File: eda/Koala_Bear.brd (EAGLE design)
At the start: 59.3 x 40 mm, 27 parts

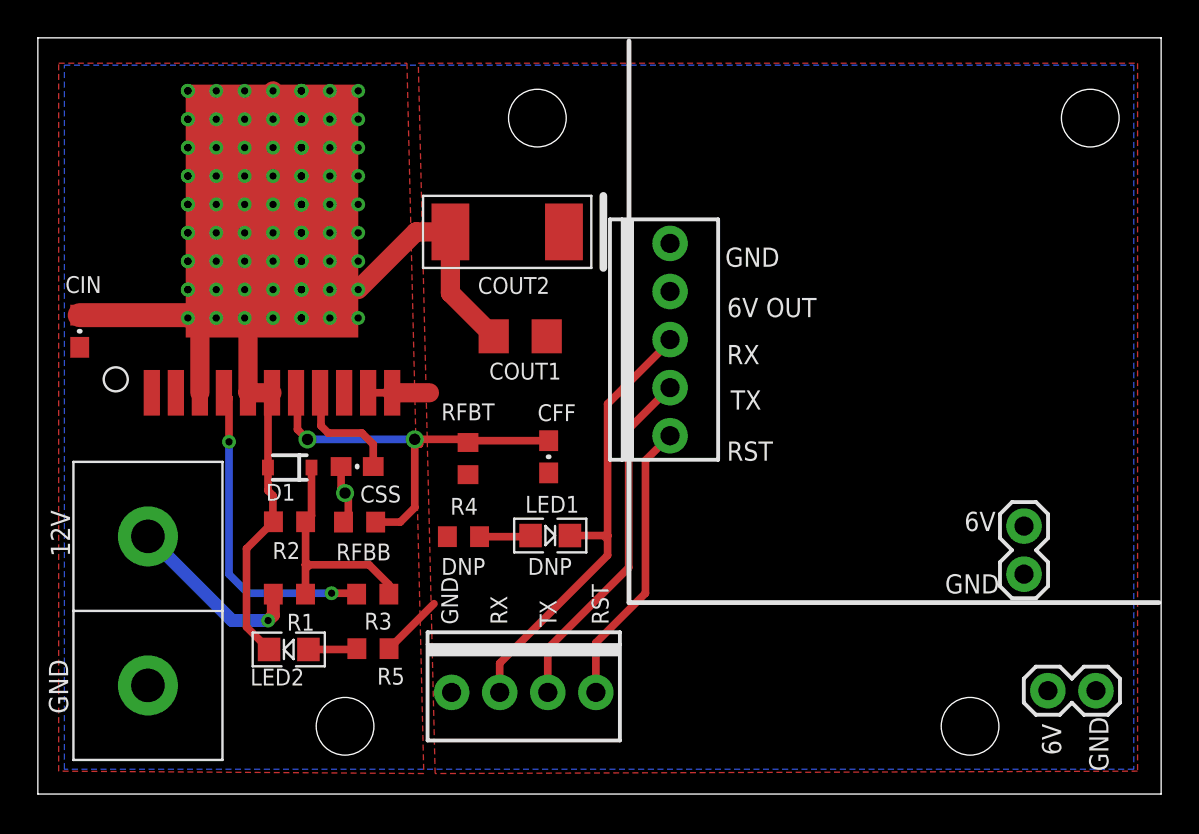
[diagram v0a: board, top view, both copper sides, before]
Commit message: Made Koala smaller
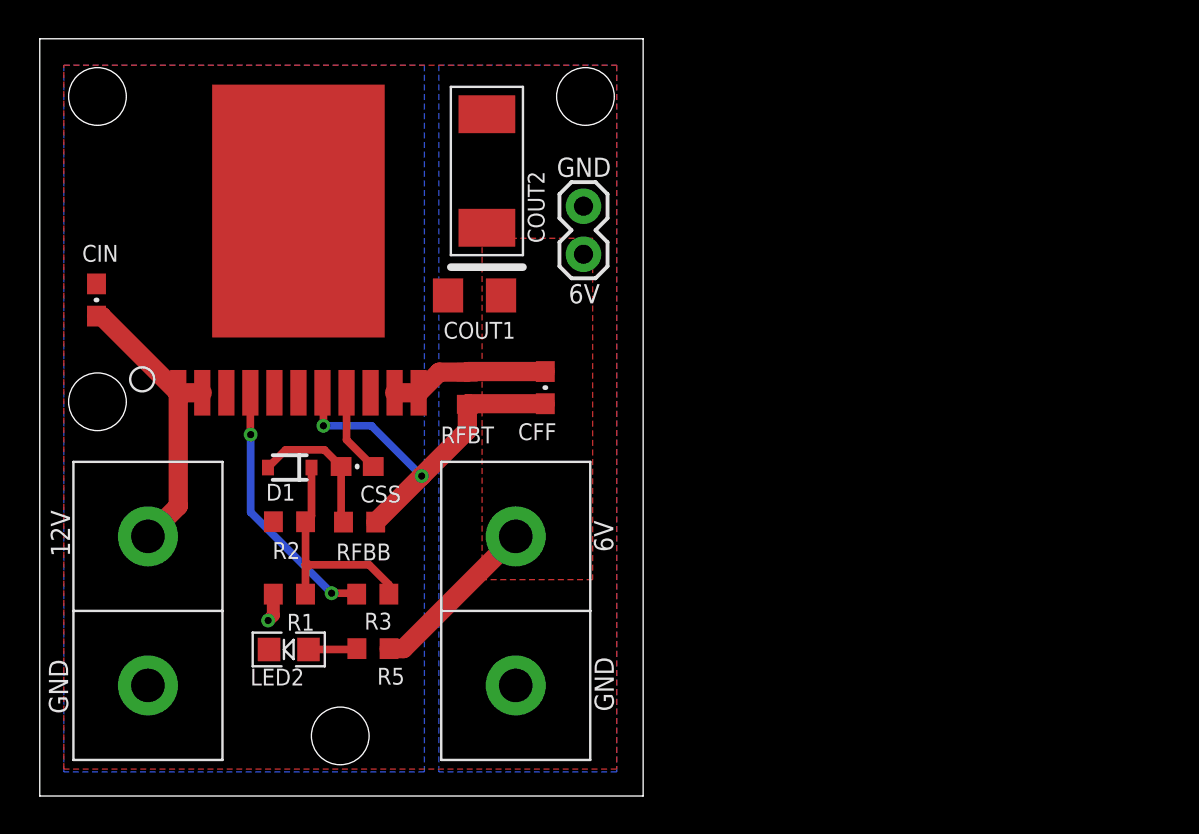
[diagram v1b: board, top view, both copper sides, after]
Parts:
- removed LED1: GRN, pie:LED-0805
- removed MSTRO_PINS: (no value), pie_new:1X04-MTA
- removed MSTRO_PWR: (no value), pie:1X05-MTA
- removed R4: 330, pie:R0603
- removed SERVO_PWR_6: (no value), pie:1X02
- added PWR1: ANDERSONVERTICAL, pie:ANDERSON_VERTICAL
- moved U$3 49.2 mm to (3.05, 20.8)
- moved SERVO_PWR_12 35.5 mm to (28.7, 29.9), turned to 270 degrees
- moved U$2 26.7 mm to (28.8, 37.0)
- moved U$11 25.9 mm to (20.8, 33.0)
- moved U$4 23.3 mm to (3.05, 37.0)
- moved U$10 19.9 mm to (5.06, 29.2)
- moved RFBT 3.72 mm to (22.6, 21.5), turned to 90 degrees
- moved CFF 3.66 mm to (26.7, 21.6), turned to 270 degrees
- moved COUT2 3.39 mm to (23.6, 33.0), turned to 90 degrees
- moved COUT1 3.24 mm to (23.0, 26.4)
- moved CIN 1.88 mm to (3.00, 26.2)
- moved U$1 1.40 mm to (13.7, 30.9)
- moved U$5 0.57 mm to (15.9, 3.17)
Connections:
- removed net N$1: LED1.A, R4.1
- removed net RST: MSTRO_PINS.4, MSTRO_PWR.1
- removed net RX: LED1.C, MSTRO_PINS.2, MSTRO_PWR.3
- removed net TX: MSTRO_PINS.3, MSTRO_PWR.2
- net GND: now also PWR1.PIN1; no longer MSTRO_PINS.1, MSTRO_PWR.5, SERVO_PWR_6.2
- net VOUT: now also PWR1.PIN2; no longer MSTRO_PWR.4, R4.2, SERVO_PWR_6.1
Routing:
- net GND: track 59.6 -> 7.69 mm, vias 90 -> 0
- net RX: track 24.4 -> 0.00 mm
- net TX: track 18.8 -> 0.00 mm
- net RST: track 15.2 -> 0.00 mm
- net VOUT: track 6.60 -> 17.6 mm
- net VIN: track 9.70 -> 17.0 mm
- net EN: track 16.9 -> 13.7 mm
- net N$1: track 3.14 -> 0.00 mm
- net FB: track 22.3 -> 20.4 mm
- net SS: track 6.10 -> 4.48 mm
- added copper zone on layer 1, net GND
- added copper zone on layer 16, net VIN
- added copper zone on layer 16, net VOUT
- removed copper zone on layer 16, net GND
- removed copper zone on layer 1, net VIN
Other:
- board size 59.3 x 40 mm -> 31.9 x 40 mm
- board text added: "Copyright (c) 2013 Pioneers in Engineering pioneers.berkeley.edu/opensource All rights reserved. Design: K Rakelly, A Hild, S Ghosh This design is open source hardware. 6/10/2014"
- board text removed: "6V OUT"
- board text removed: "Copyright (c) 2013, Pioneers in Engineering All rights reserved. Designed by: K. Rakelly and A. Hild This design is open source hardware. 12/31/2013"
- board text removed: "DNP"
- board text removed: "For more information, visit pioneers.berkeley.edu/opensource"
- board text removed: "RST"
- board text removed: "RX"
- board text removed: "TX"

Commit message: Update a bunch more part metadata
Team flag, smartsensor jig, both smartsensors, and controller now have
complete BOM information.
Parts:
- CIN: device pie:0603-CAP -> pie:1206
- LED2: value YEL -> YELLOW
- R1: value 60k -> 62k

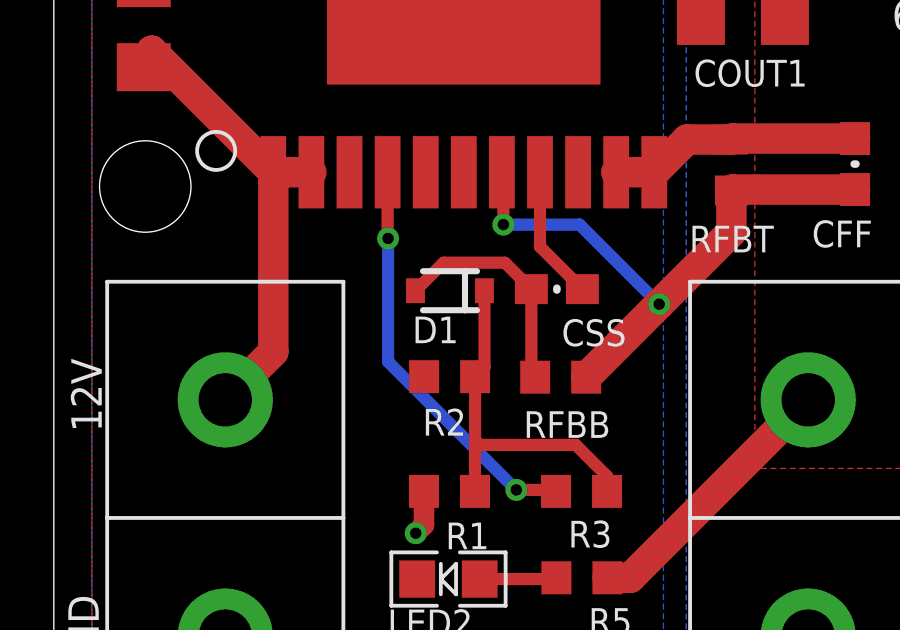
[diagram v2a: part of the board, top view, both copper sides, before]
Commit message: Move Koala parts to pie.lbr, update BOM data
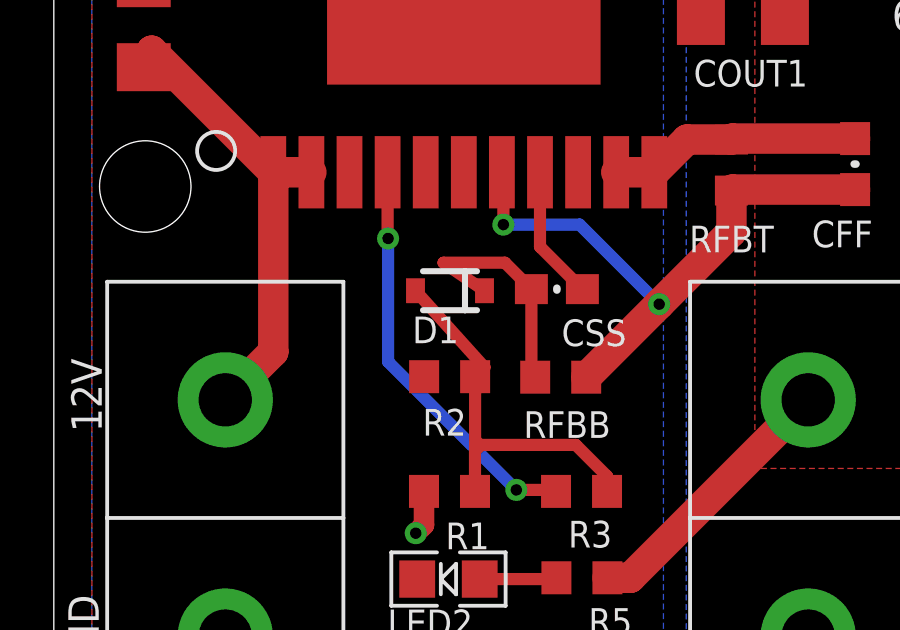
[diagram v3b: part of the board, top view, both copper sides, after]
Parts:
- CFF: value 4.7nf -> 4.7nF
- COUT1: device SparkFun:1206 -> pie:1206
- COUT2: device TANT_CASE_E:TANT_CASE_E -> pie:TANT_CASE_E
- D1: device SparkFun:SOD-323 -> pie:SOD-323
- U$1: device LMZ12010:LMZ12010 -> pie:LMZ12010
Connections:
- net DIODE: now also D1.2; no longer D1.1
- net GND: now also D1.1; no longer D1.2
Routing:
- net DIODE: track 12.2 -> 13.0 mm
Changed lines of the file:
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@@
 <layer number="1" name="Top" color="4" fill="1" visible="yes" active="yes"/>
 <layer number="2" name="Route2" color="1" fill="3" visible="no" active="no"/>
-<layer number="3" name="Route3" color="4" fill="3" visible="no" active="no"/>
-<layer number="4" name="Route4" color="1" fill="4" visible="no" active="no"/>
+<layer number="3" name="Route3" color="20" fill="3" visible="no" active="no"/>
+<layer number="4" name="Route4" color="21" fill="4" visible="no" active="no"/>
 <layer number="5" name="Route5" color="4" fill="4" visible="no" active="no"/>
 <layer number="6" name="Route6" color="1" fill="8" visible="no" active="no"/>
@@
 </autorouter>
 <elements>
-<element name="U$1" library="LMZ12010" package="LMZ12010" value="LMZ12010" x="13.666" y="30.904" smashed="yes"/>
+<element name="U$1" library="pie" package="LMZ12010" value="LMZ12010" x="13.666" y="30.904" smashed="yes">
+<attribute name="PIE-INT-REF-NUM" value="LMZ12010" x="13.666" y="30.904" size="1.778" layer="27" display="off"/>
+</element>
 <element name="R1" library="pie" package="R0603" value="62k" x="13.189" y="10.664" smashed="yes" rot="R180">
 <attribute name="NAME" x="14.518359375" y="9.626359375" size="0.889" layer="25" font="vector" ratio="20" rot="R180"/>
@@
 <attribute name="PIE-INT-REF-NUM" value="RESISTOR-GENERIC" x="16.896" y="14.472" size="1.778" layer="27" rot="R180" display="off"/>
 </element>
-<element name="CFF" library="pie" package="0603-CAP" value="4.7nf" x="26.7089125" y="21.575575" smashed="yes" rot="R270">
+<element name="CFF" library="pie" package="0603-CAP" value="4.7nF" x="26.7089125" y="21.575575" smashed="yes" rot="R270">
 <attribute name="NAME" x="25.268425" y="18.8019125" size="0.889" layer="25" font="vector" ratio="20"/>
 <attribute name="PIE-INT-REF-NUM" value="CAPACITOR-GENERIC" x="26.7089125" y="21.575575" size="1.778" layer="27" rot="R270" display="off"/>
@@
 <attribute name="PIE-INT-REF-NUM" value="CAPACITOR-GENERIC" x="2.998" y="26.205" size="1.778" layer="27" rot="R90" display="off"/>
 </element>
-<element name="COUT1" library="SparkFun" package="1206" value="47uF" x="22.970553125" y="26.445975" smashed="yes" rot="R180">
+<element name="COUT1" library="pie" package="1206" value="47uF" x="22.970553125" y="26.445975" smashed="yes" rot="R180">
 <attribute name="NAME" x="25.129553125" y="25.048975" size="0.889" layer="25" font="vector" ratio="20" rot="R180"/>
-</element>
-<element name="D1" library="SparkFun" package="SOD-323" value="5.1V" x="13.206" y="17.354" smashed="yes" rot="R180">
+<attribute name="PIE-INT-REF-NUM" value="CAPACITOR-GENERIC" x="22.970553125" y="26.445975" size="1.778" layer="27" rot="R180" display="off"/>
+</element>
+<element name="D1" library="pie" package="SOD-323" value="5.1V" x="13.206" y="17.354" smashed="yes" rot="R180">
 <attribute name="NAME" x="13.495" y="16.492" size="0.889" layer="25" font="vector" ratio="20" rot="R180"/>
-</element>
-<element name="COUT2" library="TANT_CASE_E" package="TANT_CASE_E" value="470uF" x="23.622" y="33.02" smashed="yes" rot="R90">
+<attribute name="PIE-INT-REF-NUM" value="DIODE" x="13.206" y="17.354" size="1.778" layer="27" rot="R180" display="off"/>
+</element>
+<element name="COUT2" library="pie" package="TANT_CASE_E" value="470uF" x="23.622" y="33.02" smashed="yes" rot="R90">
 <attribute name="NAME" x="26.67" y="29.21" size="0.889" layer="25" font="vector" ratio="20" rot="R90"/>
+<attribute name="PIE-INT-REF-NUM" value="CAPACITOR-TANTALUM" x="23.622" y="33.02" size="1.778" layer="27" rot="R90" display="off"/>
 </element>
 <element name="R3" library="pie" package="R0603" value="100" x="17.591" y="10.664" smashed="yes" rot="R180">
@@
 <contactref element="CIN" pad="2"/>
 <contactref element="COUT1" pad="2"/>
-<contactref element="D1" pad="2"/>
+<contactref element="D1" pad="1"/>
 <contactref element="COUT2" pad="NEG"/>
 <polygon width="0.4064" layer="1" rank="2">
@@
 <wire x1="16.046" y1="14.472" x2="15.919" y2="14.599" width="0.4064" layer="1"/>
 <wire x1="15.919" y1="14.599" x2="15.919" y2="17.407" width="0.4064" layer="1"/>
-<wire x1="12.056" y1="17.354" x2="12.99" y2="18.288" width="0.4064" layer="1"/>
+<wire x1="14.356" y1="17.354" x2="12.99" y2="18.288" width="0.4064" layer="1"/>
 <wire x1="12.99" y1="18.288" x2="15.038" y2="18.288" width="0.4064" layer="1"/>
 <wire x1="15.038" y1="18.288" x2="15.919" y2="17.407" width="0.4064" layer="1"/>
@@
 <signal name="DIODE">
 <contactref element="R2" pad="2"/>
-<contactref element="D1" pad="1"/>
+<contactref element="D1" pad="2"/>
 <contactref element="R1" pad="1"/>
 <contactref element="R3" pad="1"/>
@@
 <wire x1="14.044" y1="14.489" x2="14.044" y2="12.219" width="0.4064" layer="1"/>
 <wire x1="14.044" y1="12.219" x2="14.039" y2="12.214" width="0.4064" layer="1"/>
-<wire x1="14.356" y1="17.354" x2="14.356" y2="14.801" width="0.4064" layer="1"/>
+<wire x1="12.056" y1="17.354" x2="14.356" y2="14.801" width="0.4064" layer="1"/>
 <wire x1="14.356" y1="14.801" x2="14.044" y2="14.489" width="0.4064" layer="1"/>
 <polygon width="0.254" layer="1">

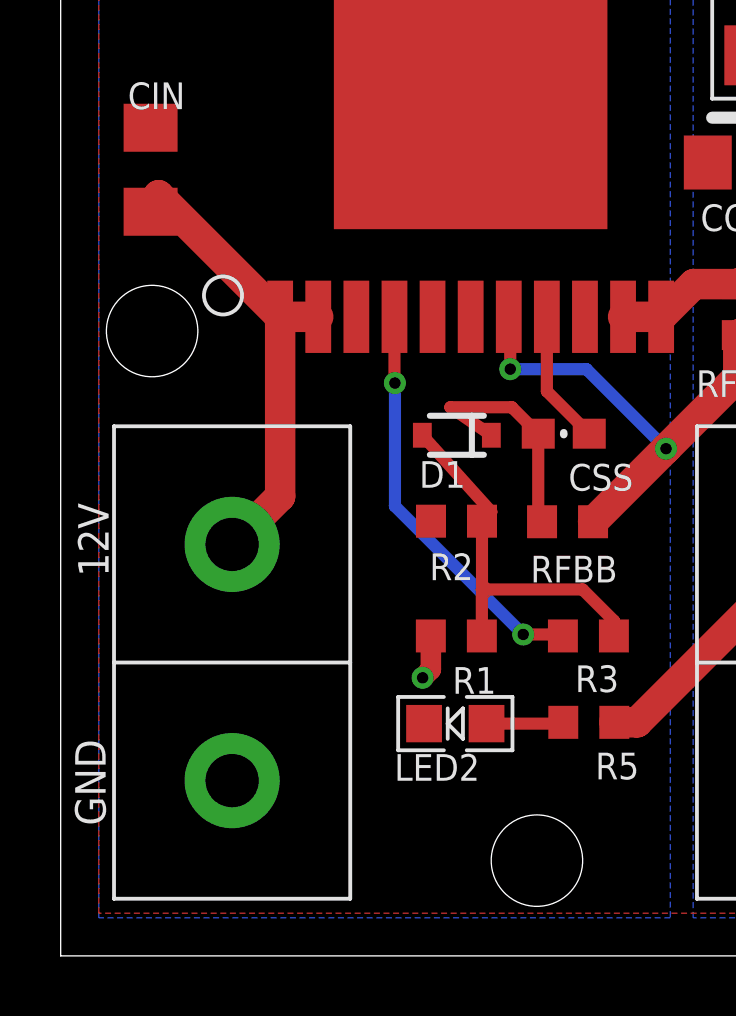
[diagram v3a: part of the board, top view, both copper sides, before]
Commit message: Correct rev, version #, and dates on all boards!
Plus a few other minor changes:
- Standardized silk screen style across jigs.
- Fixed wierd trace angles.
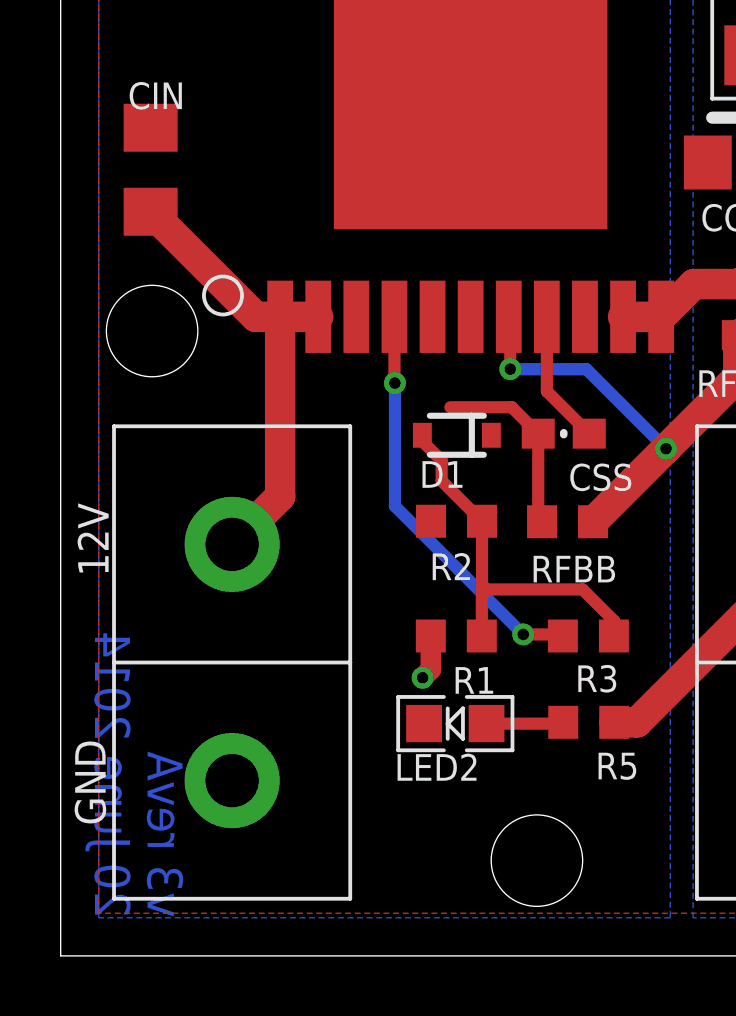
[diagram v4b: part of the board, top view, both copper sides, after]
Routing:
- net GND: track 8.03 -> 6.37 mm
- net VIN: track 17.4 -> 16.8 mm
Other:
- board text added: "PiE Robotics Buck Switching Regulator Version 3 Rev. A"
- board text added: "v3 revA 20 June 2014"
- board text removed: "PiE Robotics Buck Switching Regulator Version 2 : Revision D"
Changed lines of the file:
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@@
 <layer number="49" name="Reference" color="7" fill="1" visible="no" active="yes"/>
 <layer number="50" name="dxf" color="7" fill="1" visible="no" active="yes"/>
-<layer number="51" name="tDocu" color="6" fill="1" visible="yes" active="yes"/>
+<layer number="51" name="tDocu" color="6" fill="1" visible="no" active="yes"/>
 <layer number="52" name="bDocu" color="6" fill="1" visible="yes" active="yes"/>
 <layer number="53" name="tGND_GNDA" color="7" fill="9" visible="no" active="no"/>
@@
 <text x="24.103" y="15.848" size="1.016" layer="22" font="vector" ratio="15" rot="MR90">PiE Robotics
 Buck Switching Regulator
-Version 2 : Revision D</text>
+Version 3 Rev. A</text>
 <wire x1="31.877" y1="0" x2="0" y2="0" width="0" layer="20"/>
 <text x="1.499" y="4.344" size="1.016" layer="21" font="vector" ratio="20" rot="R90">GND</text>
@@
 <text x="30.328" y="4.471" size="1.016" layer="21" font="vector" ratio="20" rot="R90">GND</text>
 <text x="30.301" y="12.895" size="1.016" layer="21" font="vector" ratio="20" rot="R90">6V</text>
+<text x="1.143" y="1.27" size="1.1684" layer="16" font="vector" ratio="15" rot="MR90">v3 revA
+20 June 2014</text>
 </plain>
 <attributes>
@@
 <wire x1="16.046" y1="14.472" x2="15.919" y2="14.599" width="0.4064" layer="1"/>
 <wire x1="15.919" y1="14.599" x2="15.919" y2="17.407" width="0.4064" layer="1"/>
-<wire x1="14.356" y1="17.354" x2="12.99" y2="18.288" width="0.4064" layer="1"/>
 <wire x1="12.99" y1="18.288" x2="15.038" y2="18.288" width="0.4064" layer="1"/>
 <wire x1="15.038" y1="18.288" x2="15.919" y2="17.407" width="0.4064" layer="1"/>
@@
 <wire x1="7.316" y1="21.3028" x2="7.316" y2="15.317" width="1.016" layer="1"/>
 <wire x1="7.316" y1="15.317" x2="5.715" y2="13.716" width="1.016" layer="1"/>
-<wire x1="7.316" y1="21.3028" x2="3.2638" y2="25.355" width="1.016" layer="1"/>
-<wire x1="3.2638" y1="25.355" x2="2.998" y2="24.805" width="1.016" layer="1"/>
+<wire x1="7.316" y1="21.3028" x2="6.5002" y2="21.3028" width="1.016" layer="1"/>
+<wire x1="6.5002" y1="21.3028" x2="2.998" y2="24.805" width="1.016" layer="1"/>
 </signal>
 <signal name="FB">
@@
 <wire x1="14.044" y1="14.489" x2="14.044" y2="12.219" width="0.4064" layer="1"/>
 <wire x1="14.044" y1="12.219" x2="14.039" y2="12.214" width="0.4064" layer="1"/>
-<wire x1="12.056" y1="17.354" x2="14.356" y2="14.801" width="0.4064" layer="1"/>
 <wire x1="14.356" y1="14.801" x2="14.044" y2="14.489" width="0.4064" layer="1"/>
 <polygon width="0.254" layer="1">
@@
 <wire x1="17.399" y1="12.214" x2="18.441" y2="11.172" width="0.4064" layer="1"/>
 <wire x1="18.441" y1="11.172" x2="18.441" y2="10.664" width="0.4064" layer="1"/>
+<wire x1="12.056" y1="17.354" x2="12.056" y2="17.154" width="0.4064" layer="1"/>
+<wire x1="12.056" y1="17.154" x2="12.7" y2="16.51" width="0.4064" layer="1"/>
+<wire x1="12.7" y1="16.51" x2="12.7" y2="15.833" width="0.4064" layer="1"/>
+<wire x1="12.7" y1="15.833" x2="14.044" y2="14.489" width="0.4064" layer="1"/>
 </signal>
 <signal name="EN">
